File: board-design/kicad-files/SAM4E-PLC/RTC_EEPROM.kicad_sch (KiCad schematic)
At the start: 17 parts, among them U1 MCP7940N-xSN, U16 24LC512

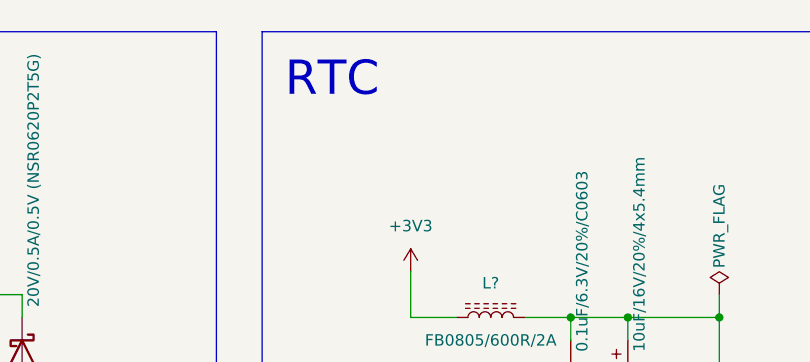
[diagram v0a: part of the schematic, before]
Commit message: [IN PROGRESS]
SAM4E-PLC PCB design in progress.

Signed-off-by: Nicolae-Andrei Vasile <vasilenicolaeandrei@gmail.com>
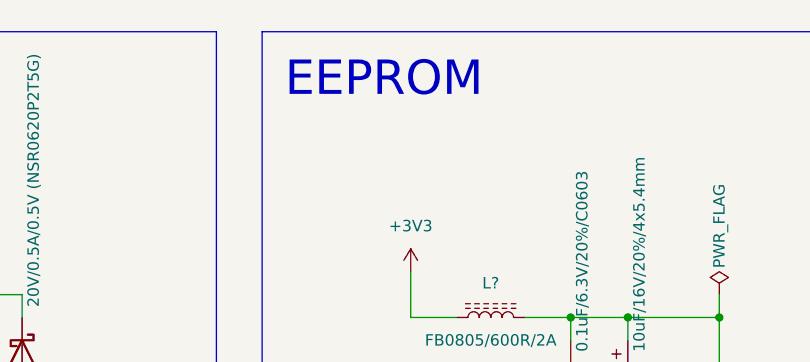
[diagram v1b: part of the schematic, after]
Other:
- note added: "EEPROM"
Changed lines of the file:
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@@
     (fill (type none))
   )
-  (text "RTC" (at 147.32 58.42 0)
+  (text "EEPROM" (at 147.32 58.42 0)
     (effects (font (size 3.81 3.81) (color 140 140 0 1)) (justify left bottom))
   )

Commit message: [UPDATE]
Work in progress.

Signed-off-by: Nicolae-Andrei Vasile <vasilenicolaeandrei@gmail.com>
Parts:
- BT1: value CR2032 (Keystone 1057) -> CR2032 (Panasonic vertical); footprint Battery:BatteryHolder_Keystone_1057_1x2032 -> Battery:Battery_Panasonic_CR2032-VS1N_Vertical_CircularHoles
- D38: renamed from D45; footprint (none) -> Diode_SMD:D_SOD-923
- U16: footprint (none) -> Package_SO:SOIC-8_3.9x4.9mm_P1.27mm
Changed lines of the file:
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@@
       (effects (font (size 1.27 1.27)))
     )
-    (property "Value" "CR2032 (Keystone 1057)" (at 107.95 97.79 90)
-      (effects (font (size 1.27 1.27)))
-    )
-    (property "Footprint" "Battery:BatteryHolder_Keystone_1057_1x2032" (at 108.204 93.98 90)
+    (property "Value" "CR2032 (Panasonic vertical)" (at 107.95 97.79 90)
+      (effects (font (size 1.27 1.27)))
+    )
+    (property "Footprint" "Battery:Battery_Panasonic_CR2032-VS1N_Vertical_CircularHoles" (at 108.204 93.98 90)
       (effects (font (size 1.27 1.27)) hide)
     )
@@
       (effects (font (size 1.27 1.27)) (justify left))
     )
-    (property "Footprint" "" (at 195.58 114.3 0)
+    (property "Footprint" "Package_SO:SOIC-8_3.9x4.9mm_P1.27mm" (at 195.58 114.3 0)
       (effects (font (size 1.27 1.27)) hide)
     )
@@
         )
         (path "/93076d8a-73da-4f5d-b7f2-28678f1db77d/fc19d0ce-fd3e-4f10-b156-7f34046be7ce"
-          (reference "R123") (unit 1)
+          (reference "R115") (unit 1)
         )
       )
@@
         )
         (path "/93076d8a-73da-4f5d-b7f2-28678f1db77d/fc19d0ce-fd3e-4f10-b156-7f34046be7ce"
-          (reference "R124") (unit 1)
+          (reference "R116") (unit 1)
         )
       )
@@
   (symbol (lib_id "Device:D_Schottky") (at 118.11 86.36 270) (unit 1)
     (in_bom yes) (on_board yes) (dnp no)
-    (property "Reference" "D45" (at 119.38 90.17 0)
+    (property "Reference" "D38" (at 119.38 90.17 0)
       (effects (font (size 1.27 1.27)))
     )
@@
       (effects (font (size 1.27 1.27)))
     )
-    (property "Footprint" "" (at 118.11 86.36 0)
+    (property "Footprint" "Diode_SMD:D_SOD-923" (at 118.11 86.36 0)
       (effects (font (size 1.27 1.27)) hide)
     )
@@
       (project "SAM4E-PLC"
         (path "/93076d8a-73da-4f5d-b7f2-28678f1db77d/fc19d0ce-fd3e-4f10-b156-7f34046be7ce"
-          (reference "D45") (unit 1)
-        )
-      )
+          (reference "D38") (unit 1)
+        )
+      )

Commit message: [UPDATE]
Work in progress.

Signed-off-by: Nicolae-Andrei Vasile <vasilenicolaeandrei@gmail.com>
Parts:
- renumbered D38 to D39
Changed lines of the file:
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@@
         )
         (path "/93076d8a-73da-4f5d-b7f2-28678f1db77d/fc19d0ce-fd3e-4f10-b156-7f34046be7ce"
-          (reference "C97") (unit 1)
+          (reference "C99") (unit 1)
         )
       )
@@
         )
         (path "/93076d8a-73da-4f5d-b7f2-28678f1db77d/fc19d0ce-fd3e-4f10-b156-7f34046be7ce"
-          (reference "C99") (unit 1)
+          (reference "C101") (unit 1)
         )
       )
@@
         )
         (path "/93076d8a-73da-4f5d-b7f2-28678f1db77d/fc19d0ce-fd3e-4f10-b156-7f34046be7ce"
-          (reference "C100") (unit 1)
+          (reference "C102") (unit 1)
         )
       )
@@
         )
         (path "/93076d8a-73da-4f5d-b7f2-28678f1db77d/fc19d0ce-fd3e-4f10-b156-7f34046be7ce"
-          (reference "C101") (unit 1)
+          (reference "C103") (unit 1)
         )
       )
@@
         )
         (path "/93076d8a-73da-4f5d-b7f2-28678f1db77d/fc19d0ce-fd3e-4f10-b156-7f34046be7ce"
-          (reference "C102") (unit 1)
+          (reference "C104") (unit 1)
         )
       )
@@
         )
         (path "/93076d8a-73da-4f5d-b7f2-28678f1db77d/fc19d0ce-fd3e-4f10-b156-7f34046be7ce"
-          (reference "#PWR088") (unit 1)
+          (reference "#PWR089") (unit 1)
         )
       )
@@
         )
         (path "/93076d8a-73da-4f5d-b7f2-28678f1db77d/fc19d0ce-fd3e-4f10-b156-7f34046be7ce"
-          (reference "C96") (unit 1)
+          (reference "C98") (unit 1)
         )
       )
@@
         )
         (path "/93076d8a-73da-4f5d-b7f2-28678f1db77d/fc19d0ce-fd3e-4f10-b156-7f34046be7ce"
-          (reference "#PWR094") (unit 1)
+          (reference "#PWR095") (unit 1)
         )
       )
@@
         )
         (path "/93076d8a-73da-4f5d-b7f2-28678f1db77d/fc19d0ce-fd3e-4f10-b156-7f34046be7ce"
-          (reference "C98") (unit 1)
+          (reference "C100") (unit 1)
         )
       )
@@
         )
         (path "/93076d8a-73da-4f5d-b7f2-28678f1db77d/fc19d0ce-fd3e-4f10-b156-7f34046be7ce"
-          (reference "C103") (unit 1)
+          (reference "C105") (unit 1)
         )
       )
@@
         )
         (path "/93076d8a-73da-4f5d-b7f2-28678f1db77d/fc19d0ce-fd3e-4f10-b156-7f34046be7ce"
-          (reference "#PWR091") (unit 1)
+          (reference "#PWR092") (unit 1)
         )
       )
@@
         )
         (path "/93076d8a-73da-4f5d-b7f2-28678f1db77d/fc19d0ce-fd3e-4f10-b156-7f34046be7ce"
-          (reference "#PWR089") (unit 1)
+          (reference "#PWR090") (unit 1)
         )
       )
@@
         )
         (path "/93076d8a-73da-4f5d-b7f2-28678f1db77d/fc19d0ce-fd3e-4f10-b156-7f34046be7ce"
-          (reference "#PWR090") (unit 1)
+          (reference "#PWR091") (unit 1)
         )
       )
@@
   (symbol (lib_id "Device:D_Schottky") (at 118.11 86.36 270) (unit 1)
     (in_bom yes) (on_board yes) (dnp no)
-    (property "Reference" "D38" (at 119.38 90.17 0)
+    (property "Reference" "D39" (at 119.38 90.17 0)
       (effects (font (size 1.27 1.27)))
     )
@@
       (project "SAM4E-PLC"
         (path "/93076d8a-73da-4f5d-b7f2-28678f1db77d/fc19d0ce-fd3e-4f10-b156-7f34046be7ce"
-          (reference "D38") (unit 1)
+          (reference "D39") (unit 1)
         )
       )
@@
         )
         (path "/93076d8a-73da-4f5d-b7f2-28678f1db77d/fc19d0ce-fd3e-4f10-b156-7f34046be7ce"
-          (reference "#PWR087") (unit 1)
+          (reference "#PWR088") (unit 1)
         )
       )
@@
         )
         (path "/93076d8a-73da-4f5d-b7f2-28678f1db77d/fc19d0ce-fd3e-4f10-b156-7f34046be7ce"
-          (reference "#PWR092") (unit 1)
+          (reference "#PWR093") (unit 1)
         )
       )
@@
         )
         (path "/93076d8a-73da-4f5d-b7f2-28678f1db77d/fc19d0ce-fd3e-4f10-b156-7f34046be7ce"
-          (reference "#PWR093") (unit 1)
-        )
-      )
+          (reference "#PWR094") (unit 1)
+        )
+      )
